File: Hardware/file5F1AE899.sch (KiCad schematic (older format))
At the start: 8 parts, among them U5 SPF5189Z

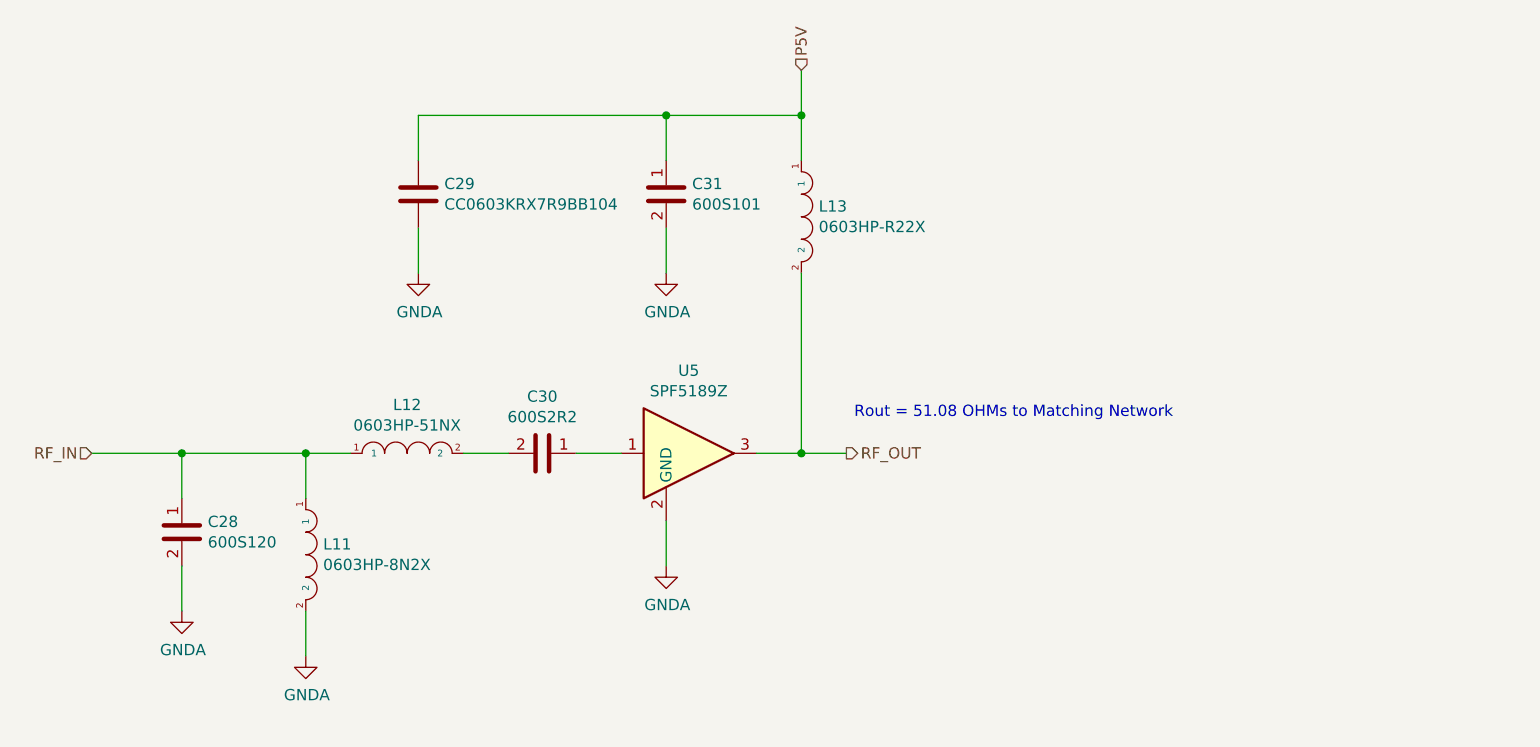
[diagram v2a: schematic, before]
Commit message: Improving LNA simulations and Documentation package. More to come on this one.
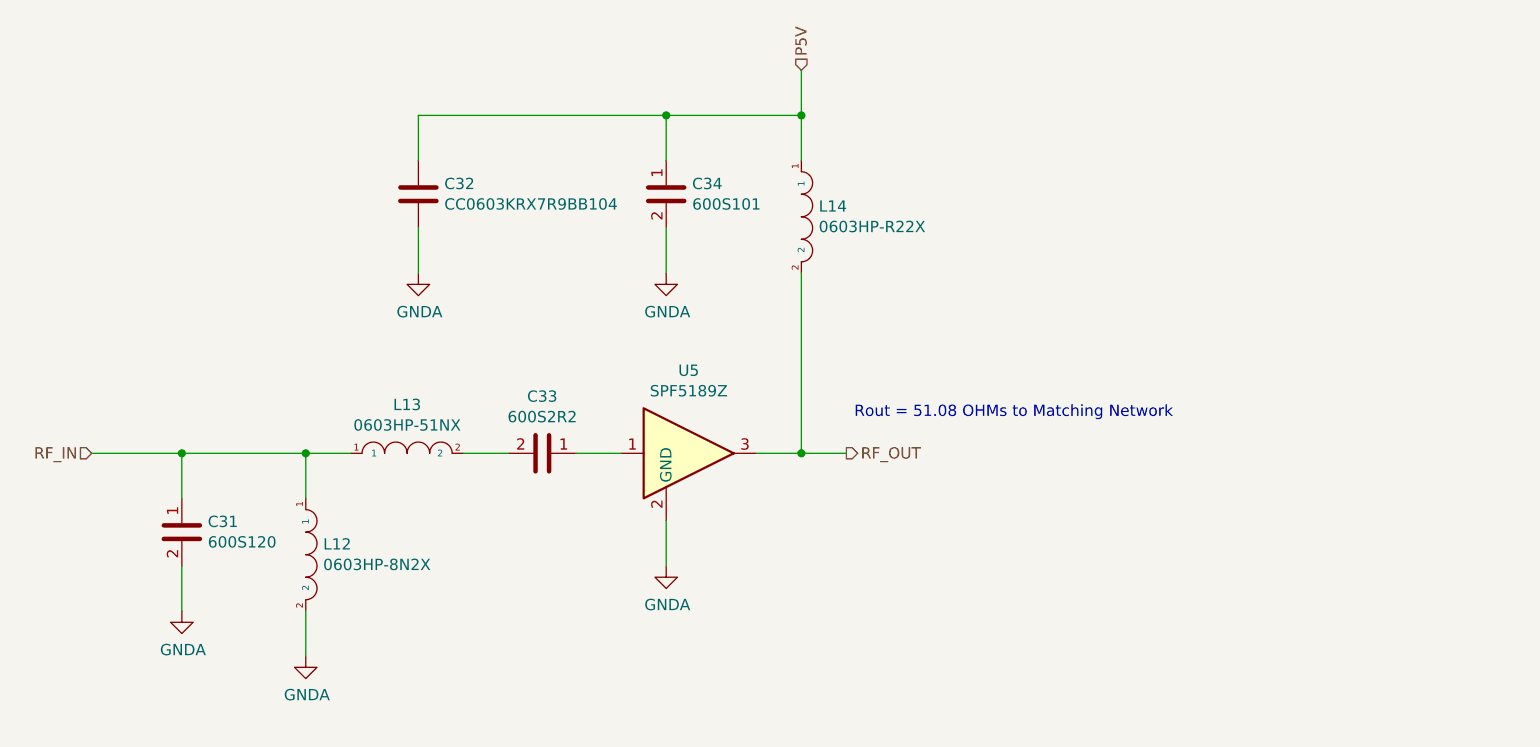
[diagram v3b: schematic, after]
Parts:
- renumbered C28 to C31, C29 to C32, C30 to C33, C31 to C34, L11 to L12, L12 to L13, L13 to L14
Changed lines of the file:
@@
 $Descr A4 11693 8268
 encoding utf-8
-Sheet 17 24
+Sheet 17 23
 Title ""
 Date ""
@@
 AR Path="/5F04F5B6/5F1BCDB1" Ref="#PWR?"  Part="1"
 AR Path="/5F04F5B6/5F1AE89A/5F1BCDB1" Ref="#PWR?"  Part="1"
-AR Path="/5F204DEC/5F205D8E/5F1AE89A/5F1BCDB1" Ref="#PWR035"  Part="1"
-F 0 "#PWR035" H 4500 4600 50  0001 C CNN
+AR Path="/5F204DEC/5F205D8E/5F1AE89A/5F1BCDB1" Ref="#PWR037"  Part="1"
+F 0 "#PWR037" H 4500 4600 50  0001 C CNN
 F 1 "GNDA" H 4505 4677 50  0000 C CNN
 F 2 "" H 4500 4850 50  0001 C CNN
@@
 AR Path="/5F04F5B6/5F1BCDB7" Ref="#PWR?"  Part="1"
 AR Path="/5F04F5B6/5F1AE89A/5F1BCDB7" Ref="#PWR?"  Part="1"
-AR Path="/5F204DEC/5F205D8E/5F1AE89A/5F1BCDB7" Ref="#PWR038"  Part="1"
-F 0 "#PWR038" H 6100 4200 50  0001 C CNN
+AR Path="/5F204DEC/5F205D8E/5F1AE89A/5F1BCDB7" Ref="#PWR040"  Part="1"
+F 0 "#PWR040" H 6100 4200 50  0001 C CNN
 F 1 "GNDA" H 6105 4277 50  0000 C CNN
 F 2 "" H 6100 4450 50  0001 C CNN
@@
 AR Path="/5F04F5B6/5F1BCDC4" Ref="#PWR?"  Part="1"
 AR Path="/5F04F5B6/5F1AE89A/5F1BCDC4" Ref="#PWR?"  Part="1"
-AR Path="/5F204DEC/5F205D8E/5F1AE89A/5F1BCDC4" Ref="#PWR034"  Part="1"
-F 0 "#PWR034" H 3950 4400 50  0001 C CNN
+AR Path="/5F204DEC/5F205D8E/5F1AE89A/5F1BCDC4" Ref="#PWR036"  Part="1"
+F 0 "#PWR036" H 3950 4400 50  0001 C CNN
 F 1 "GNDA" H 3955 4477 50  0000 C CNN
 F 2 "" H 3950 4650 50  0001 C CNN
@@
 AR Path="/5F04F5B6/5F1BCDCB" Ref="L?"  Part="1"
 AR Path="/5F04F5B6/5F1AE89A/5F1BCDCB" Ref="L?"  Part="1"
-AR Path="/5F204DEC/5F205D8E/5F1AE89A/5F1BCDCB" Ref="L13"  Part="1"
-F 0 "L13" V 6654 2977 50  0000 L CNN
+AR Path="/5F204DEC/5F205D8E/5F1AE89A/5F1BCDCB" Ref="L14"  Part="1"
+F 0 "L14" V 6654 2977 50  0000 L CNN
 F 1 "0603HP-R22X" V 6745 2977 50  0000 L CNN
 F 2 "Resistor_SMD:R_0603_1608Metric" H 6450 3050 50  0001 C CNN
@@
 AR Path="/5F04F5B6/5F1BCDDC" Ref="C?"  Part="1"
 AR Path="/5F04F5B6/5F1AE89A/5F1BCDDC" Ref="C?"  Part="1"
-AR Path="/5F204DEC/5F205D8E/5F1AE89A/5F1BCDDC" Ref="C30"  Part="1"
-F 0 "C30" V 5298 3950 50  0000 C CNN
+AR Path="/5F204DEC/5F205D8E/5F1AE89A/5F1BCDDC" Ref="C33"  Part="1"
+F 0 "C33" V 5298 3950 50  0000 C CNN
 F 1 "600S2R2" V 5389 3950 50  0000 C CNN
 F 2 "Resistor_SMD:R_0603_1608Metric" H 5600 4050 50  0001 C CNN
@@
 AR Path="/5F04F5B6/5F1BCDE2" Ref="L?"  Part="1"
 AR Path="/5F04F5B6/5F1AE89A/5F1BCDE2" Ref="L?"  Part="1"
-AR Path="/5F204DEC/5F205D8E/5F1AE89A/5F1BCDE2" Ref="L12"  Part="1"
-F 0 "L12" H 4950 4165 50  0000 C CNN
+AR Path="/5F204DEC/5F205D8E/5F1AE89A/5F1BCDE2" Ref="L13"  Part="1"
+F 0 "L13" H 4950 4165 50  0000 C CNN
 F 1 "0603HP-51NX" H 4950 4074 50  0000 C CNN
 F 2 "Resistor_SMD:R_0603_1608Metric" H 4700 4100 50  0001 C CNN
@@
 AR Path="/5F04F5B6/5F1BCDE8" Ref="L?"  Part="1"
 AR Path="/5F04F5B6/5F1AE89A/5F1BCDE8" Ref="L?"  Part="1"
-AR Path="/5F204DEC/5F205D8E/5F1AE89A/5F1BCDE8" Ref="L11"  Part="1"
-F 0 "L11" V 4454 4477 50  0000 L CNN
+AR Path="/5F204DEC/5F205D8E/5F1AE89A/5F1BCDE8" Ref="L12"  Part="1"
+F 0 "L12" V 4454 4477 50  0000 L CNN
 F 1 "0603HP-8N2X" V 4545 4477 50  0000 L CNN
 F 2 "Resistor_SMD:R_0603_1608Metric" H 4250 4550 50  0001 C CNN
@@
 AR Path="/5F04F5B6/5F1BCDEE" Ref="C?"  Part="1"
 AR Path="/5F04F5B6/5F1AE89A/5F1BCDEE" Ref="C?"  Part="1"
-AR Path="/5F204DEC/5F205D8E/5F1AE89A/5F1BCDEE" Ref="C28"  Part="1"
-F 0 "C28" H 4065 4346 50  0000 L CNN
+AR Path="/5F204DEC/5F205D8E/5F1AE89A/5F1BCDEE" Ref="C31"  Part="1"
+F 0 "C31" H 4065 4346 50  0000 L CNN
 F 1 "600S120" H 4065 4255 50  0000 L CNN
 F 2 "Resistor_SMD:R_0603_1608Metric" H 4000 4400 50  0001 C CNN
@@
 AR Path="/5F04F5B6/5F1BCDFD" Ref="C?"  Part="1"
 AR Path="/5F04F5B6/5F1AE89A/5F1BCDFD" Ref="C?"  Part="1"
-AR Path="/5F204DEC/5F205D8E/5F1AE89A/5F1BCDFD" Ref="C31"  Part="1"
-F 0 "C31" H 6215 2846 50  0000 L CNN
+AR Path="/5F204DEC/5F205D8E/5F1AE89A/5F1BCDFD" Ref="C34"  Part="1"
+F 0 "C34" H 6215 2846 50  0000 L CNN
 F 1 "600S101" H 6215 2755 50  0000 L CNN
 F 2 "Resistor_SMD:R_0603_1608Metric" H 6150 2900 50  0001 C CNN
@@
 AR Path="/5F04F5B6/5F1BCE03" Ref="#PWR?"  Part="1"
 AR Path="/5F04F5B6/5F1AE89A/5F1BCE03" Ref="#PWR?"  Part="1"
-AR Path="/5F204DEC/5F205D8E/5F1AE89A/5F1BCE03" Ref="#PWR036"  Part="1"
-F 0 "#PWR036" H 5000 2900 50  0001 C CNN
+AR Path="/5F204DEC/5F205D8E/5F1AE89A/5F1BCE03" Ref="#PWR038"  Part="1"
+F 0 "#PWR038" H 5000 2900 50  0001 C CNN
 F 1 "GNDA" H 5005 2977 50  0000 C CNN
 F 2 "" H 5000 3150 50  0001 C CNN
@@
 AR Path="/5F04F5B6/5F1BCE0A" Ref="#PWR?"  Part="1"
 AR Path="/5F04F5B6/5F1AE89A/5F1BCE0A" Ref="#PWR?"  Part="1"
-AR Path="/5F204DEC/5F205D8E/5F1AE89A/5F1BCE0A" Ref="#PWR037"  Part="1"
-F 0 "#PWR037" H 6100 2900 50  0001 C CNN
+AR Path="/5F204DEC/5F205D8E/5F1AE89A/5F1BCE0A" Ref="#PWR039"  Part="1"
+F 0 "#PWR039" H 6100 2900 50  0001 C CNN
 F 1 "GNDA" H 6105 2977 50  0000 C CNN
 F 2 "" H 6100 3150 50  0001 C CNN
@@
 AR Path="/5F04F5B6/5F1BCE11" Ref="C?"  Part="1"
 AR Path="/5F04F5B6/5F1AE89A/5F1BCE11" Ref="C?"  Part="1"
-AR Path="/5F204DEC/5F205D8E/5F1AE89A/5F1BCE11" Ref="C29"  Part="1"
-F 0 "C29" H 5115 2846 50  0000 L CNN
+AR Path="/5F204DEC/5F205D8E/5F1AE89A/5F1BCE11" Ref="C32"  Part="1"
+F 0 "C32" H 5115 2846 50  0000 L CNN
 F 1 "CC0603KRX7R9BB104" H 5115 2755 50  0000 L CNN
 F 2 "Capacitor_SMD:C_0603_1608Metric" H 5038 2650 50  0001 C CNN
